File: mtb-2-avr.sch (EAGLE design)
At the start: 18 parts, among them IC1 MEGA8A-AU, Q1/2 14.745 MHz, Q2 14.745 MHz

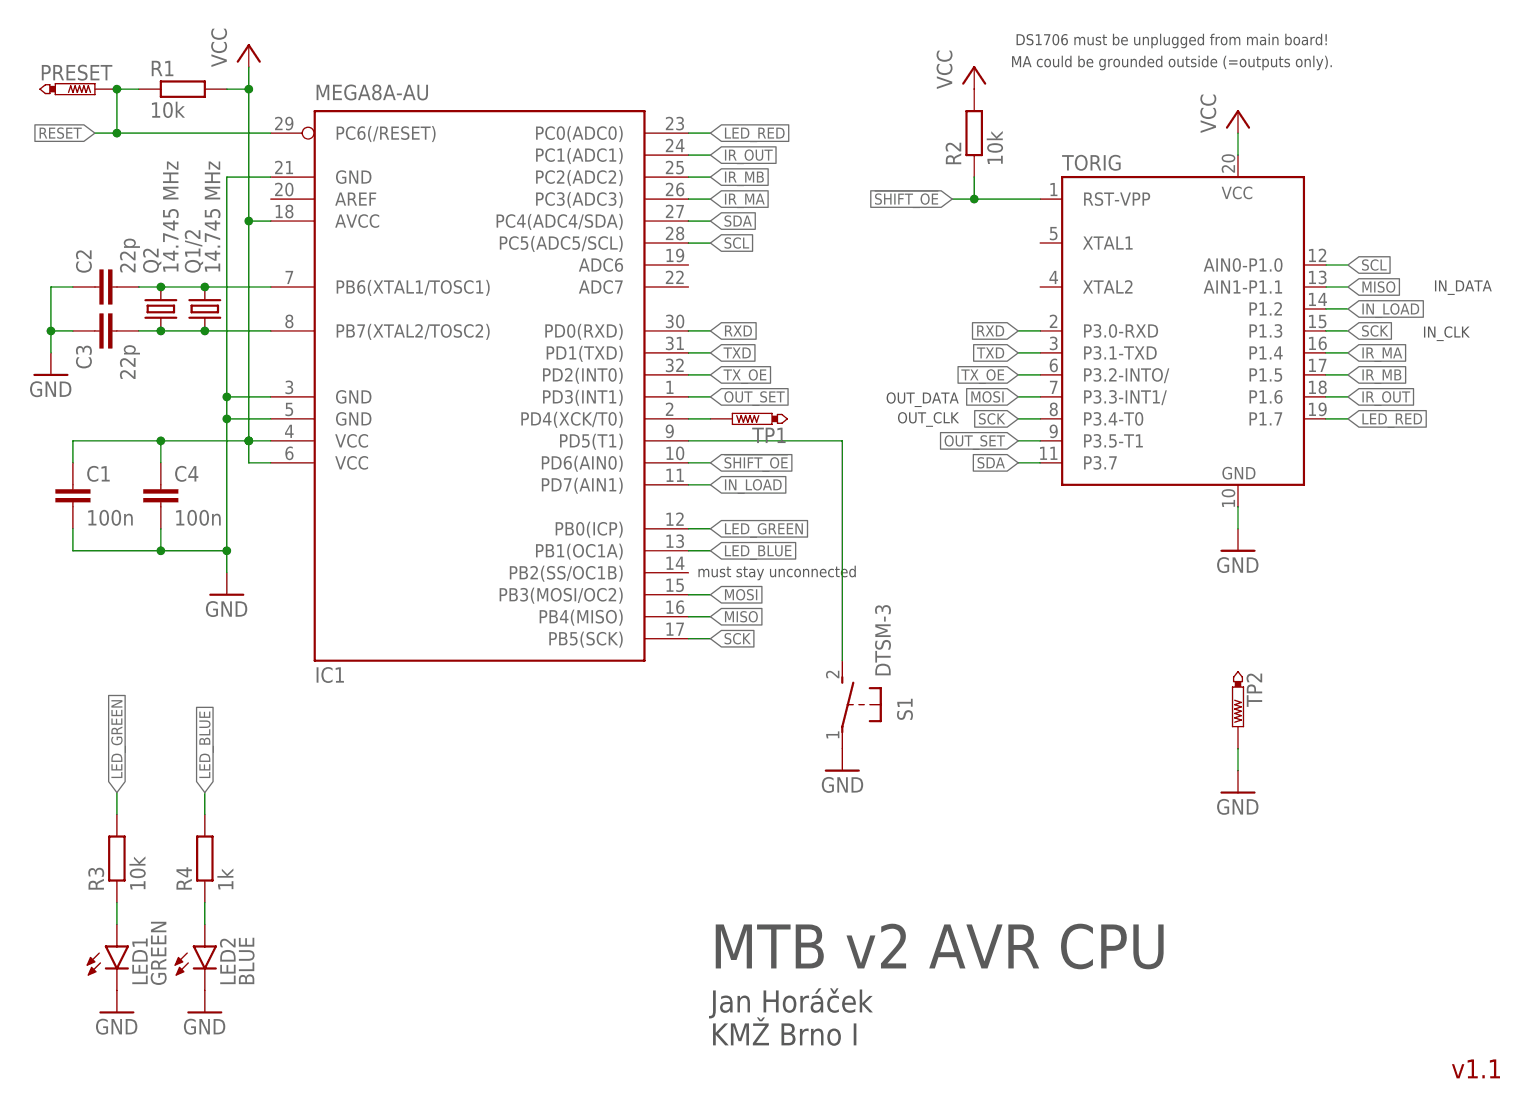
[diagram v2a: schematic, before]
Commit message: Add pull-up on TX_OE.
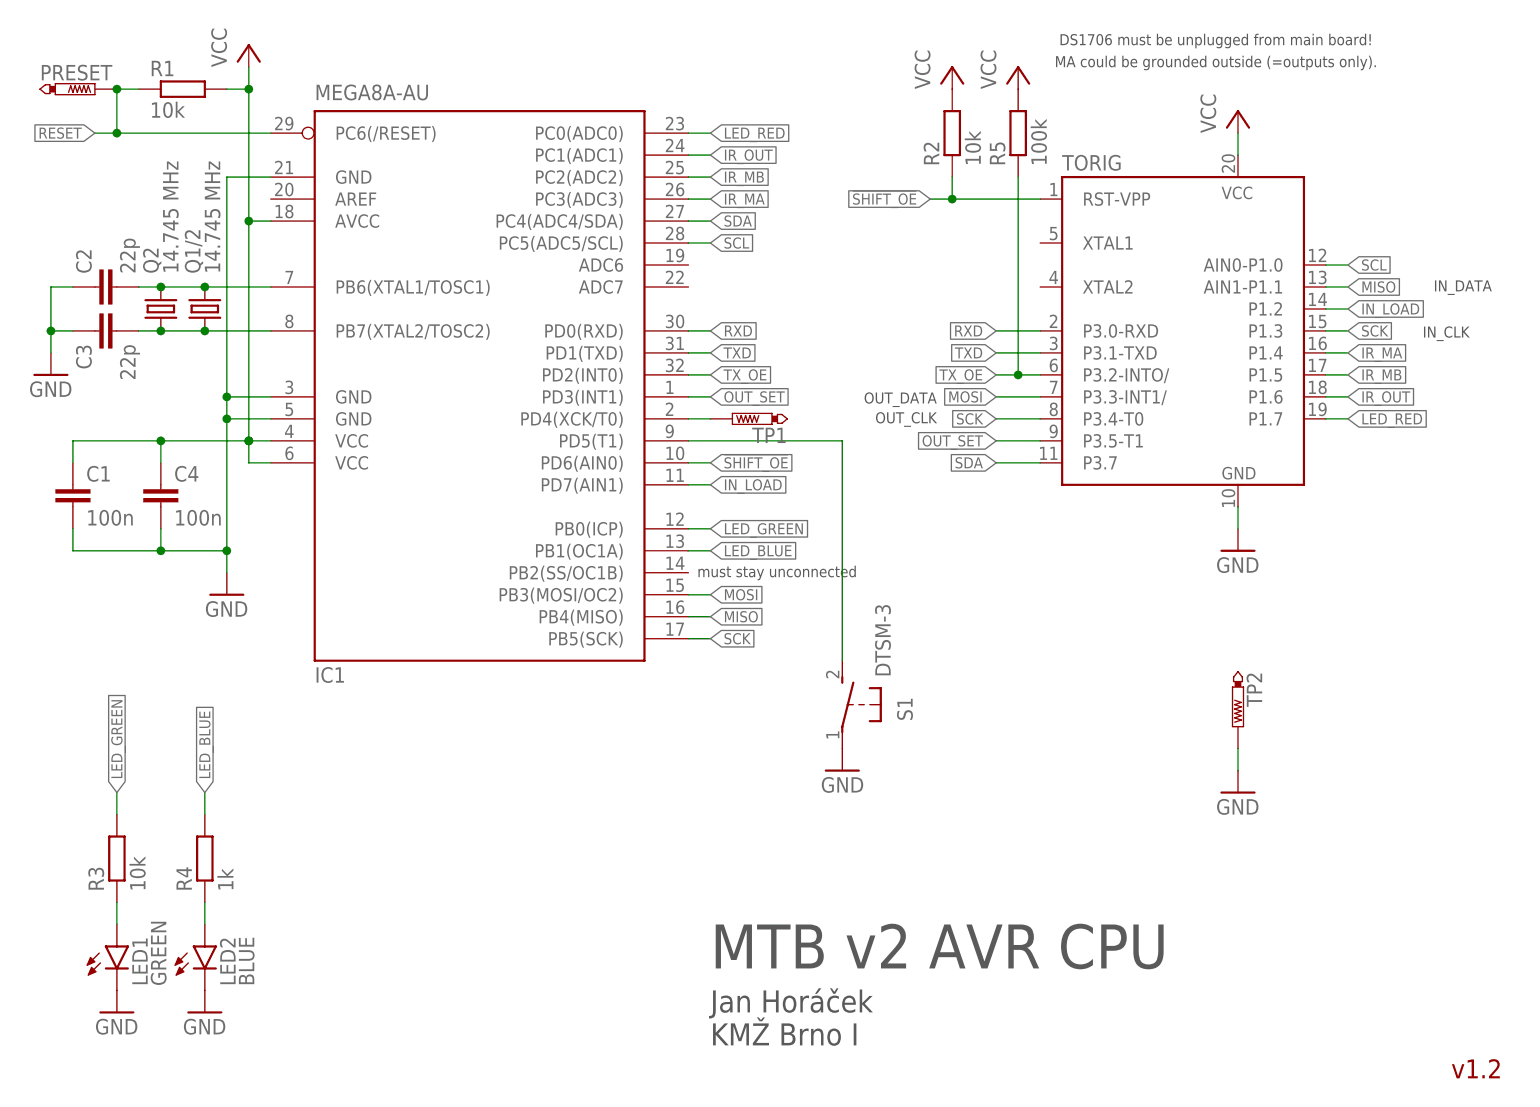
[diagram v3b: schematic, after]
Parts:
- added R5: 100k, rcl:R-EU_R0603
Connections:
- net TX_OE: now also R5.1
- net VCC: now also R5.2
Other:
- note added: "v1.2"
- note removed: "v1.1"
- moved on the sheet: R2

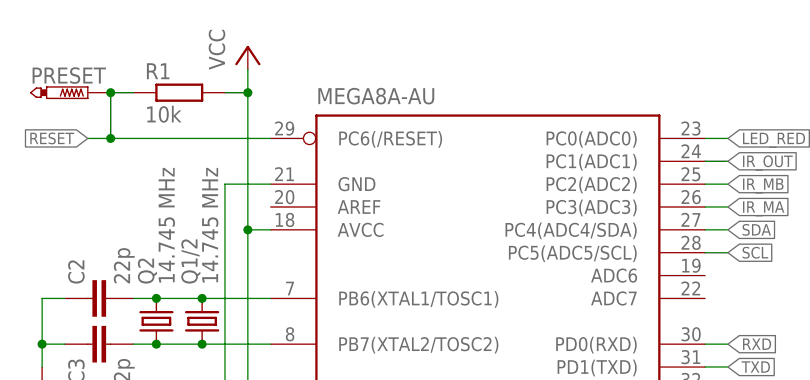
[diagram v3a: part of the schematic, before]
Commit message: Use ATmega328.
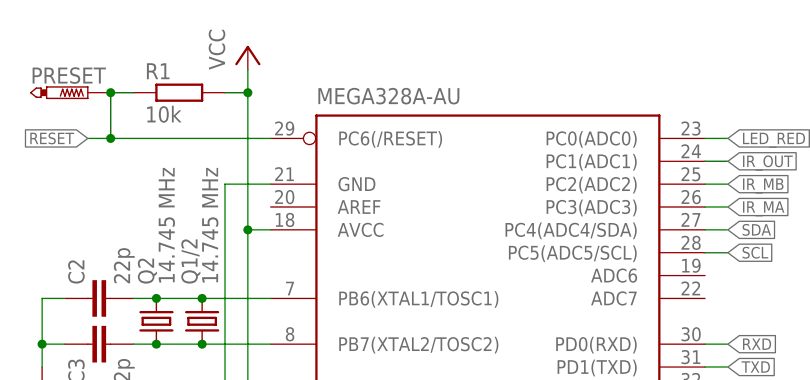
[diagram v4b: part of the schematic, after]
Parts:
- IC1: value MEGA8A-AU -> MEGA328A-AU; LCSC_PART C16190 -> C14877
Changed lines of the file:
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@@
 <part name="P+1" library="supply1" library_urn="urn:adsk.eagle:library:371" deviceset="VCC" device=""/>
 <part name="GND1" library="supply1" library_urn="urn:adsk.eagle:library:371" deviceset="GND" device=""/>
-<part name="IC1" library="atmel" library_urn="urn:adsk.eagle:library:105" deviceset="MEGA8" device="-AI" package3d_urn="urn:adsk.eagle:package:4313/2" value="MEGA8A-AU">
-<attribute name="LCSC_PART" value="C16190"/>
+<part name="IC1" library="atmel" library_urn="urn:adsk.eagle:library:105" deviceset="MEGA8" device="-AI" package3d_urn="urn:adsk.eagle:package:4313/2" value="MEGA328A-AU">
+<attribute name="LCSC_PART" value="C14877"/>
 </part>
 <part name="C1" library="rcl" deviceset="C-EU" device="C0603" value="100n">

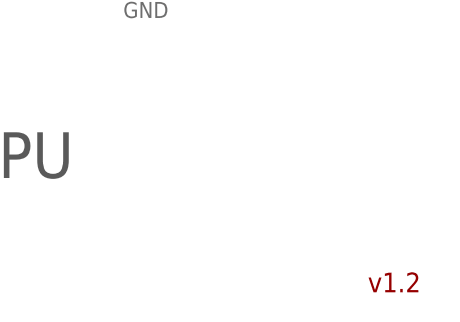
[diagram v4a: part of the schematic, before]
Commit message: Change outer dimensions to fit to MTB-TTL.
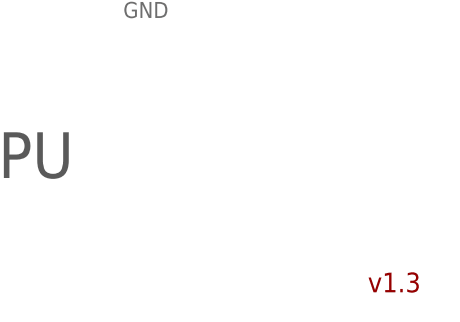
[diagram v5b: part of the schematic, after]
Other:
- note added: "v1.3"
- note removed: "v1.2"
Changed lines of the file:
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@@
 <text x="86.36" y="8.89" size="2.54" layer="97">Jan Horáček
 KMŽ Brno I</text>
-<text x="171.958" y="5.08" size="2.1844" layer="94">v1.2</text>
+<text x="171.958" y="5.08" size="2.1844" layer="94">v1.3</text>
 <text x="144.78" y="124.46" size="1.27" layer="97" align="bottom-center">DS1706 must be unplugged from main board!</text>
 <text x="144.78" y="121.92" size="1.27" layer="97" align="bottom-center">MA could be grounded outside (=outputs only).</text>
